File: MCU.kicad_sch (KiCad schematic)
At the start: 87 parts, among them J301 Conn_ARM_JTAG_SWD_20, U1 W9825G6KH-6, U12 USBLC6-2P6, U15 ISOM8115, U18 STM32H7R7I8Tx, U2 W25Q128JVS, U3 FM24CL64B, U301 STM32N657I0H3Q, Y1 ASDLJ-E-49.152MHZ-L-R-T

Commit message: imrt1176 is added
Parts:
- removed C112, C113, C114, C115, C149, C150, C151, C152: 2.2uF, PCM_JLCPCB:C_0402, symbol PCM_JLCPCB-Capacitors:0402,2.2uF
- removed C116, C118, C127, C58, C64, C73: 1uF, PCM_JLCPCB:C_0402, symbol PCM_JLCPCB-Capacitors:0402,1uF
- removed C117, C119, C121, C122, C123, C124, C125, C126, C128, C130, C132, C133, C134, C136, C137, C138, C140, C141, C142, C143, C144, C145, C146, C59, C76, C77: 100nF, PCM_JLCPCB:C_0402, symbol PCM_JLCPCB-Capacitors:0402,100nF
- removed C120, C135, C139, C148: 4.7uF, PCM_JLCPCB:C_0402, symbol PCM_JLCPCB-Capacitors:0402,4.7uF
- removed C147, C153: 10uF, PCM_JLCPCB:C_0603, symbol PCM_JLCPCB-Capacitors:0603,10uF
- removed C154: 220pF, PCM_JLCPCB:C_0402, symbol PCM_JLCPCB-Capacitors:0402,220pF
- removed D2: SMF6.0CA, PCM_JLCPCB:D_SOD-123FL, symbol PCM_JLCPCB-Diodes:TVS-Bi,SMF6.0CA
- removed J301: Conn_ARM_JTAG_SWD_20, Connector_PinSocket_1.27mm:PinSocket_2x10_P1.27mm_Horizontal, symbol Connector:Conn_ARM_JTAG_SWD_20
- removed L1: Choke_Wurth_WE-CNSW_744232090, Inductor_SMD:L_CommonMode_Wurth_WE-CNSW-1206, symbol Filter:Choke_Wurth_WE-CNSW_744232090
- removed L6: 2.2u, Inductor_SMD:L_1206_3216Metric, symbol Device:L
- removed NT1, NT10, NT3, NT4, NT5, NT6, NT7, NT8, NT9: ~, NetTie:NetTie-2_SMD_Pad0.5mm, symbol Device:NetTie_2
- removed R1: 0Ω, PCM_JLCPCB:R_0402, symbol PCM_JLCPCB-Resistors:0402,0Ω
- removed R10, R11: 56kΩ, PCM_JLCPCB:R_0402, symbol PCM_JLCPCB-Resistors:0402,56kΩ
- removed R2: 220Ω, PCM_JLCPCB:R_0805, symbol PCM_JLCPCB-Resistors:0805,220Ω
- removed R35, R40, R45: 33Ω, PCM_JLCPCB:R_0402, symbol PCM_JLCPCB-Resistors:0402,33Ω
- removed R36: 4.7kΩ, PCM_JLCPCB:R_0402, symbol PCM_JLCPCB-Resistors:0402,4.7kΩ
- removed R39: 10kΩ, PCM_JLCPCB:R_0402, symbol PCM_JLCPCB-Resistors:0402,10kΩ
- removed R5: 2kΩ, PCM_JLCPCB:R_0402, symbol PCM_JLCPCB-Resistors:0402,2kΩ
- removed R98: 47Ω, PCM_JLCPCB:R_0402, symbol PCM_JLCPCB-Resistors:0402,47Ω
- removed U15: ISOM8115, Package_SO:SOIC-4_4.55x2.6mm_P1.27mm, symbol Isolator:EL814
- removed U18: STM32H7R7I8Tx, Package_QFP:LQFP-176_24x24mm_P0.5mm, symbol MCU_ST_STM32H7:STM32H7R7I8Tx
- removed U301: STM32N657I0H3Q, User:VFBGA178_12X12_STM, symbol User:STM32N657I0H3Q
- added C15, C16, C59: 1uF, PCM_JLCPCB:C_0402, symbol PCM_JLCPCB-Capacitors:0402,1uF
- added R1, R15: 5.1kΩ, PCM_JLCPCB:R_0402, symbol PCM_JLCPCB-Resistors:0402,5.1kΩ
- added R9: 4.7kΩ, PCM_JLCPCB:R_0402, symbol PCM_JLCPCB-Resistors:0402,4.7kΩ
- added U10: ISOUSB111DWXR, symbol User:ISOUSB111DWXR
- added U6: MIMXRT1176CVM8A, User:BGA289C80P17X17_1400X1400X152, symbol User:MIMXRT1176CVM8A
- added Y3: SG-5032CAN 24MHz, Oscillator:Oscillator_SMD_SeikoEpson_SG8002LB-4Pin_5.0x3.2mm, symbol Oscillator:SG-5032CAN
- Y1: value ASDLJ-E-49.152MHZ-L-R-T -> ASDLJ-E-24.576MHZ-L-R-T
- renumbered C155 to C46, C10 to C57, R116 to R13, R15 to R14, R19 to R16
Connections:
- net +3.3V: now also C15.2, C16.2, U10.14 (3.3V2), U10.16 (VBUS2), Y3.1 (~{ST}), Y3.4 (VCC)
- net CC: now also R15.1
- net D+: now also U12.4 (I/O2); no longer U12.6 (I/O1)
- net D-: now also U12.6 (I/O1); no longer U12.4 (I/O2)
- net FLASH_CLK: now also U6.G14 (GPIO_SD_B2_07)
- net FLASH_QSPI0: now also U6.F15 (GPIO_SD_B2_08)
- net FLASH_QSPI1: now also U6.H15 (GPIO_SD_B2_09)
- net FLASH_QSPI2: now also U6.H14 (GPIO_SD_B2_10)
- net FLASH_QSPI3: now also U6.F16 (GPIO_SD_B2_11)
- net FLASH_~{CS}: now also U6.F17 (GPIO_SD_B2_06)
- net GND: now also C15.1, C16.1, R9.2, U10.15 (GND2), U10.9 (GND2), Y3.2 (GND); no longer C14.2, U12.2 (GND)
- net I2S_CK: now also U6.K12 (GPIO_AD_22)
- net I2S_WS: now also U6.J12 (GPIO_AD_23)
- net RAM_A0: now also U6.A3 (GPIO_EMC_B1_09)
- net RAM_A1: now also U6.A2 (GPIO_EMC_B1_10)
- net RAM_A10: now also U6.B2 (GPIO_EMC_B1_23)
- net RAM_A11: now also U6.C4 (GPIO_EMC_B1_19)
- net RAM_A12: now also U6.C3 (GPIO_EMC_B1_20)
- net RAM_A2: now also U6.C2 (GPIO_EMC_B1_11)
- net RAM_A3: now also U6.C5 (GPIO_EMC_B1_12)
- net RAM_A4: now also U6.D5 (GPIO_EMC_B1_13)
- net RAM_A5: now also U6.B1 (GPIO_EMC_B1_14)
- net RAM_A6: now also U6.C1 (GPIO_EMC_B1_15)
- net RAM_A7: now also U6.D3 (GPIO_EMC_B1_16)
- net RAM_A8: now also U6.B3 (GPIO_EMC_B1_17)
- net RAM_A9: now also U6.B4 (GPIO_EMC_B1_18)
- net RAM_BA0: now also U6.G2 (GPIO_EMC_B1_21)
- net RAM_BA1: now also U6.H2 (GPIO_EMC_B1_22)
- net RAM_CKE: now also U6.G5 (GPIO_EMC_B1_27)
- net RAM_CLK: now also U6.J3 (GPIO_EMC_B1_26)
- net RAM_D0: now also U6.F3 (GPIO_EMC_B1_00)
- net RAM_D1: now also U6.F2 (GPIO_EMC_B1_01)
- net RAM_D10: now also U6.D1 (GPIO_EMC_B1_32)
- net RAM_D11: now also U6.E2 (GPIO_EMC_B1_33)
- net RAM_D12: now also U6.E1 (GPIO_EMC_B1_34)
- net RAM_D13: now also U6.F1 (GPIO_EMC_B1_35)
- net RAM_D14: now also U6.G1 (GPIO_EMC_B1_36)
- net RAM_D15: now also U6.H1 (GPIO_EMC_B1_37)
- net RAM_D2: now also U6.G4 (GPIO_EMC_B1_02)
- net RAM_D3: now also U6.E4 (GPIO_EMC_B1_03)
- net RAM_D4: now also U6.H5 (GPIO_EMC_B1_04)
- net RAM_D5: now also U6.F4 (GPIO_EMC_B1_05)
- net RAM_D6: now also U6.H4 (GPIO_EMC_B1_06)
- net RAM_D7: now also U6.H3 (GPIO_EMC_B1_07)
- net RAM_D8: now also U6.E3 (GPIO_EMC_B1_30)
- net RAM_D9: now also U6.D2 (GPIO_EMC_B1_31)
- net RAM_DQMH: now also U6.J1 (GPIO_EMC_B1_38)
- net RAM_DQML: now also U6.F5 (GPIO_EMC_B1_08)
- net RAM_~{CAS}: now also U6.J5 (GPIO_EMC_B1_24)
- net RAM_~{CS}: now also U6.E6 (GPIO_EMC_B1_29)
- net RAM_~{RAS}: now also U6.J4 (GPIO_EMC_B1_25)
- net RAM_~{WE}: now also U6.E5 (GPIO_EMC_B1_28)
- net VBUS: now also C59.1, U10.1 (VBUS1); no longer C14.1
- net VBUS_DETECT: now also U10.12 (V1OK), U6.D17 (USB1_VBUS)
- net VCONN: now also R1.1
- net AUDIOCLK: now reaches Y1.3 (Out)
- net AUDIOCLK: now also U6.N15 (GPIO_AD_17)
- net at U12.1 (I/O1): now also U10.6 (UD-)
- net at U12.3 (I/O2): now also U10.7 (UD+)
- new net: C14.1, U10.3 (3.3V1)
- new net D_iso+: U10.10 (DD+), U6.E17 (USB1_DP)
- new net D_iso-: U10.11 (DD-), U6.E16 (USB1_DN)
- new net ENC1_PHASE_A: U6.R1 (GPIO_EMC_B2_03)
- new net ENC1_PHASE_B: U6.P1 (GPIO_EMC_B2_08)
- new net I2S_RX: U6.K13 (GPIO_AD_20)
- new net I2S_TX: U6.K14 (GPIO_AD_21)
- new net ISO_GND: C14.2, C59.2, R1.2, R15.2, U10.2 (GND1), U10.8 (GND1), U12.2 (GND)
- new net JTAG_MOD: R9.1, U6.U6 (GPIO_LPSR_13)
- new net JTAG_TCK: U6.T6 (GPIO_LPSR_14)
- new net JTAG_TDI: U6.U5 (GPIO_LPSR_12)
- new net JTAG_TDO: U6.T5 (GPIO_LPSR_11)
- new net JTAG_TMS: U6.U7 (GPIO_LPSR_15)
- new net JTAG_TRSTB: U6.R5 (GPIO_LPSR_10)
- new net MCU_CLOCK: U6.U16 (XTALI), Y3.3 (OUT)
- new net SPDIF_IN_UNUSED: U6.D9 (GPIO_DISP_B2_10)
- new net SPDIF_OUT_UNUSED: U6.A6 (GPIO_DISP_B2_11)
- no-connect marks 2 -> 9
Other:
- moved on the sheet: C46, C57, R117, R13, R14, R16, U12, U2, Y1

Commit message: added renesas RA8P1
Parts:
- removed C46, C67: 100nF, PCM_JLCPCB:C_0402, symbol PCM_JLCPCB-Capacitors:0402,100nF
- removed R117: 10kΩ, PCM_JLCPCB:R_0402, symbol PCM_JLCPCB-Resistors:0402,10kΩ
- removed R9: 4.7kΩ, PCM_JLCPCB:R_0402, symbol PCM_JLCPCB-Resistors:0402,4.7kΩ
- removed U2: W25Q128JVS, Package_SO:SOIC-8_5.3x5.3mm_P1.27mm, symbol Memory_Flash:W25Q128JVS
- removed U6: MIMXRT1176CVM8A, User:BGA289C80P17X17_1400X1400X152, symbol User:MIMXRT1176CVM8A
- added C46, C67, C76, C77, C78, C80: 4.7uF, PCM_JLCPCB:C_0402, symbol PCM_JLCPCB-Capacitors:0402,4.7uF
- added IC2: R7KA8P1KFLCAB#UC0, User:BGA-225_15x15_11.0x11.0mm, symbol User:R7KA8P1KFLCAB#UC0
- added JP1: BOOT_Sel, Jumper:SolderJumper-2_P1.3mm_Open_RoundedPad1.0x1.5mm, symbol Jumper:SolderJumper_2_Open
- added R31: 10kΩ, PCM_JLCPCB:R_0402, symbol PCM_JLCPCB-Resistors:0402,10kΩ
- added R34: 1.5kΩ, PCM_JLCPCB:R_0402, symbol PCM_JLCPCB-Resistors:0402,1.5kΩ
- added R55: 10kΩ, PCM_JLCPCB:R_0402x4, symbol PCM_JLCPCB-Resistors:0402x4,10kΩ
- added U2: IS25LX512M-JHLE, Package_BGA:BGA-24_6x8mm_Layout5x5_P1.0mm, symbol User:IS25LX512M-JHLE
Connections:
- net +3.3V: now also R14.2, C46.1, C67.1, C76.1, C77.1, C78.1, C80.1, R31.1, R55.1, R55.2, R55.3, R55.4, U2.B4 (VCC), U2.D1 (VCC), U2.E4 (VCC); no longer R14.1
- net AUDIOCLK: now also IC2.D9 (AUDIO_CLK)
- net D_iso+: now also IC2.R14 (P814/USB_DP)
- net D_iso-: now also IC2.P14 (P815/USB_DM)
- net FLASH_CLK: now also IC2.R5 (OSPI_CLK), U2.B2 (CLK)
- net FLASH_~{CS}: now also IC2.L4 (OSPI_CS0), R55.5, U2.C2 (~{CS})
- net FRAM_SCL: now also R14.1, IC2.L12 (FRAM_SCL0); no longer R16.2
- net FRAM_SDA: now also R16.2, IC2.L10 (FRAM_SDA0); no longer R14.2
- net FRAM_WP: now also IC2.L11 (P414)
- net Footswitch_1: now also IC2.R10 (ADC1_8)
- net Footswitch_2: now also IC2.M9 (ADC1_7)
- net GND: now also C46.2, C67.2, C76.2, C77.2, C78.2, C80.2, R34.2, U2.B3 (VSS), U2.C1 (VSS), U2.E5 (VSS)
- net GPO: now also IC2.F11 (P700)
- net I2S_CK: now also IC2.H11 (I2S_BCK0)
- net I2S_RX: now also IC2.E14 (I2S_RXD0)
- net I2S_TX: now also IC2.E11 (I2S_TXD0)
- net I2S_WS: now also IC2.G11 (I2S_LRCK0)
- net JTAG_TCK: now also IC2.C8 (P211/TCK/SWCLK)
- net JTAG_TDI: now also IC2.D6 (P208/TDI)
- net JTAG_TDO: now also IC2.D8 (P209/TDO/SWO)
- net JTAG_TMS: now also IC2.C7 (P210/TMS/SWDIO)
- net MCU_CLOCK: now also IC2.J15 (P212/EXTAL)
- net Potentiometer_1: now also IC2.R12 (ADC0_0)
- net Potentiometer_2: now also IC2.N11 (ADC0_1)
- net Potentiometer_3: now also IC2.P11 (ADC0_2)
- net Potentiometer_4: now also IC2.P12 (ADC0_3)
- net Potentiometer_5: now also IC2.R11 (ADC0_4)
- net Potentiometer_6: now also IC2.N10 (ADC0_5)
- net RAM_A0: now also IC2.G1 (SDRAM_A1)
- net RAM_A1: now also IC2.G4 (SDRAM_A2)
- net RAM_A10: now also IC2.J4 (SDRAM_A11)
- net RAM_A11: now also IC2.K4 (SDRAM_A12)
- net RAM_A12: now also IC2.J2 (SDRAM_A13)
- net RAM_A2: now also IC2.G2 (SDRAM_A3)
- net RAM_A3: now also IC2.G3 (SDRAM_A4)
- net RAM_A4: now also IC2.H1 (SDRAM_A5)
- net RAM_A5: now also IC2.H2 (SDRAM_A7)
- net RAM_A6: now also IC2.H3 (SDRAM_A6)
- net RAM_A7: now also IC2.H4 (SDRAM_A8)
- net RAM_A8: now also IC2.J1 (SDRAM_A9)
- net RAM_A9: now also IC2.J3 (SDRAM_A10)
- net RAM_BA0: now also IC2.K2 (SDRAM_A14)
- net RAM_BA1: now also IC2.K3 (SDRAM_A15)
- net RAM_CKE: now also IC2.F1 (SDRAM_CKE)
- net RAM_CLK: now also IC2.E1 (SDRAM_SDCLK)
- net RAM_D0: now also IC2.B5 (SDRAM_DQ0)
- net RAM_D1: now also IC2.C5 (SDRAM_DQ1)
- net RAM_D10: now also IC2.C3 (SDRAM_DQ10)
- net RAM_D11: now also IC2.D4 (SDRAM_DQ11)
- net RAM_D12: now also IC2.B1 (SDRAM_DQ12)
- net RAM_D13: now also IC2.C2 (SDRAM_DQ13)
- net RAM_D14: now also IC2.C1 (SDRAM_DQ14)
- net RAM_D15: now also IC2.D2 (SDRAM_DQ15)
- net RAM_D2: now also IC2.A5 (SDRAM_DQ2)
- net RAM_D3: now also IC2.A4 (SDRAM_DQ3)
- net RAM_D4: now also IC2.B4 (SDRAM_DQ4)
- net RAM_D5: now also IC2.A3 (SDRAM_DQ5)
- net RAM_D6: now also IC2.B3 (SDRAM_DQ6)
- net RAM_D7: now also IC2.C4 (SDRAM_DQ7)
- net RAM_D8: now also IC2.A2 (SDRAM_DQ8)
- net RAM_D9: now also IC2.B2 (SDRAM_DQ9)
- net RAM_DQMH: now also IC2.F3 (SDRAM_DQM1)
- net RAM_DQML: now also IC2.D3 (SDRAM_DQM0)
- net RAM_~{CAS}: now also IC2.E4 (SDRAM_CAS)
- net RAM_~{CS}: now also IC2.E3 (SDRAM_SDCS)
- net RAM_~{RAS}: now also IC2.F2 (SDRAM_RAS)
- net RAM_~{WE}: now also IC2.E2 (SDRAM_WE)
- net Switch_1A: now also IC2.M8 (ADC1_9)
- net Switch_1B: now also IC2.P10 (ADC1_6)
- net Switch_2A: now also IC2.R7 (ADC0_14)
- net Switch_2B: now also IC2.P7 (ADC1_15)
- net VBUS_DETECT: now also IC2.K12 (P407/USB_VBUS)
- net ~{RESET}: now also IC2.C6 (RES)
- new net: JP1.1 (A), R34.1
- new net BOOT_MODE: IC2.D7 (P201/MD), JP1.2 (B), R31.2
- new net FLASH_DS: IC2.M6 (OSPI_DQS), U2.C3 (DS)
- new net FLASH_OSPI0: IC2.R6 (OSPI_D0), U2.D3 (D0)
- new net FLASH_OSPI1: IC2.M7 (OSPI_D1), U2.D2 (D1)
- new net FLASH_OSPI2: IC2.N4 (OSPI_D2), U2.C4 (D2)
- new net FLASH_OSPI3: IC2.N5 (OSPI_D3), U2.D4 (D3)
- new net FLASH_OSPI4: IC2.M5 (OSPI_D4), U2.D5 (D4)
- new net FLASH_OSPI5: IC2.P6 (OSPI_D5), U2.E3 (D5)
- new net FLASH_OSPI6: IC2.N6 (OSPI_D6), U2.E2 (D6)
- new net FLASH_OSPI7: IC2.N7 (OSPI_D7), U2.E1 (D7)
- new net FLASH_~{INT}: IC2.L7 (OSPI_ECSINT1), R55.6, U2.A5 (~{INT})
- new net FLASH_~{RST}: IC2.L5 (OSPI_RESET), R55.7, R55.8, U2.A4 (~{RST})
- no-connect marks 9 -> 20
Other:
- note added: "0: USB boot 1: JTAG/Flash boot"
- note removed: "3.3V - 25mA"
- moved on the sheet: C57, R13, R14, R15, R16, Y1, Y3

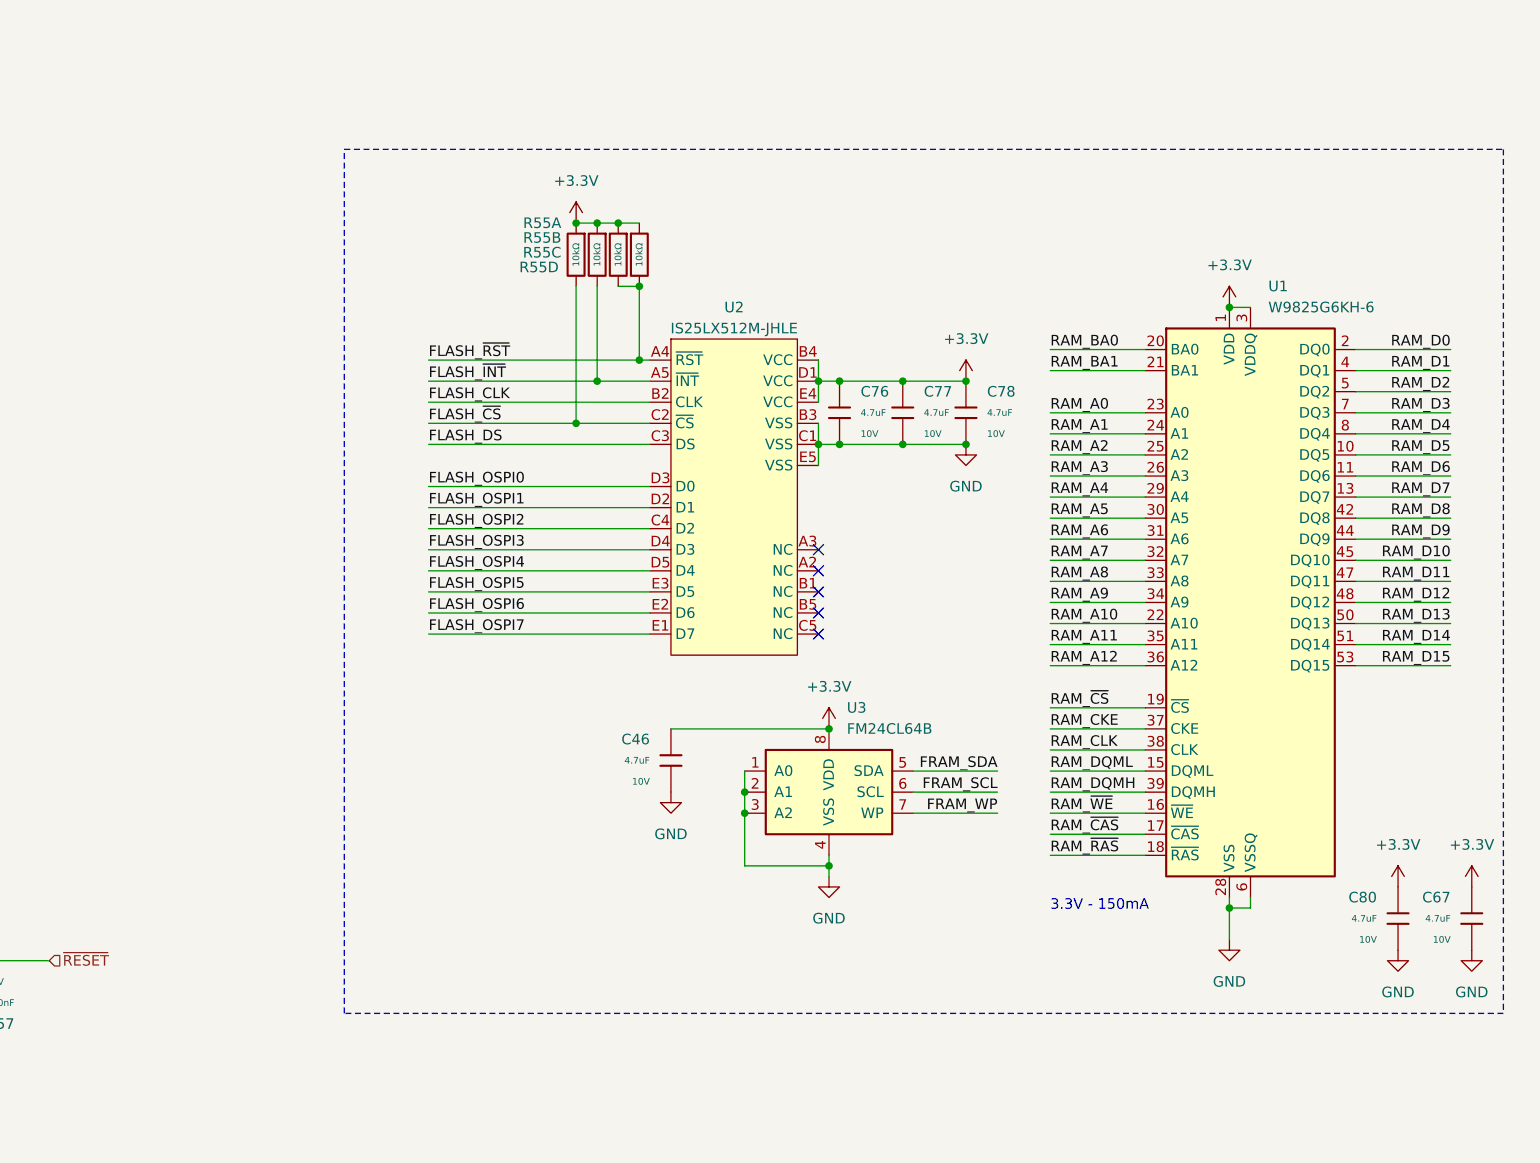
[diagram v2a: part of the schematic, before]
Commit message: progressed with SDRAM layout
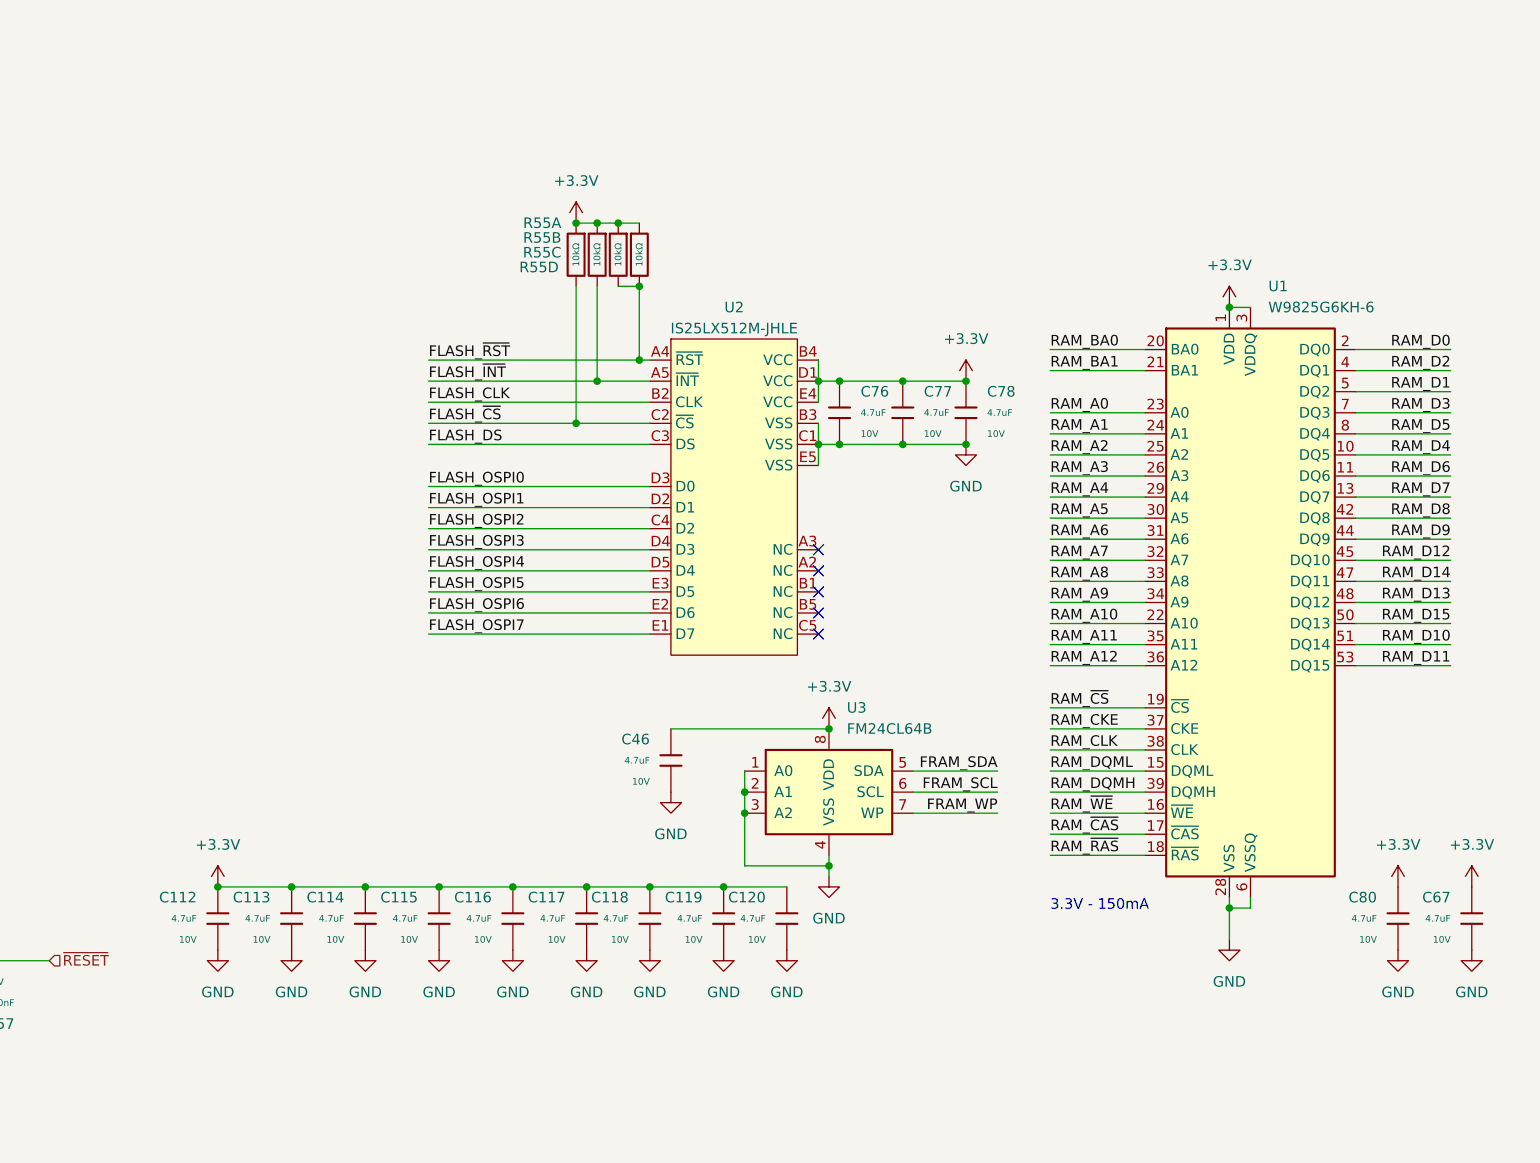
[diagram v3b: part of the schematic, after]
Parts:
- added C112, C113, C114, C115, C116, C117, C118, C119, C120: 4.7uF, PCM_JLCPCB:C_0402, symbol PCM_JLCPCB-Capacitors:0402,4.7uF
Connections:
- net +3.3V: now also C112.1, C113.1, C114.1, C115.1, C116.1, C117.1, C118.1, C119.1, C120.1
- net GND: now also C112.2, C113.2, C114.2, C115.2, C116.2, C117.2, C118.2, C119.2, C120.2
- net RAM_D1: now also U1.5 (DQ2); no longer U1.4 (DQ1)
- net RAM_D10: now also U1.51 (DQ14); no longer U1.45 (DQ10)
- net RAM_D11: now also U1.53 (DQ15); no longer U1.47 (DQ11)
- net RAM_D12: now also U1.45 (DQ10); no longer U1.48 (DQ12)
- net RAM_D13: now also U1.48 (DQ12); no longer U1.50 (DQ13)
- net RAM_D14: now also U1.47 (DQ11); no longer U1.51 (DQ14)
- net RAM_D15: now also U1.50 (DQ13); no longer U1.53 (DQ15)
- net RAM_D2: now also U1.4 (DQ1); no longer U1.5 (DQ2)
- net RAM_D4: now also U1.10 (DQ5); no longer U1.8 (DQ4)
- net RAM_D5: now also U1.8 (DQ4); no longer U1.10 (DQ5)

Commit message: layout progress
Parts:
- removed C46: 4.7uF, PCM_JLCPCB:C_0402, symbol PCM_JLCPCB-Capacitors:0402,4.7uF
- added C88: 1uF, PCM_JLCPCB:C_0402, symbol PCM_JLCPCB-Capacitors:0402,1uF
- added D11, D12, D13, D14, D15, D16, D17, D18, D19: H5VL10B, PCM_JLCPCB:D_DFN1006-2L, symbol PCM_JLCPCB-Diodes:TVS-Bi,H5VL10B
- added J1: UI Board Connector, Connector_SMD_Wurth:J_Wurth_WR-MM_690367280676, symbol Connector_Generic:Conn_01x06
- added R29: 47Ω, PCM_JLCPCB:R_0402, symbol PCM_JLCPCB-Resistors:0402,47Ω
- U10: footprint (none) -> User:SOIC16_DW_TEX-L
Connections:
- net +3.3V: now also D16.1, D19.1, J1.5 (Pin_5)
- net D+: now also U12.6 (I/O1); no longer U12.4 (I/O2)
- net D-: now also U12.4 (I/O2); no longer U12.6 (I/O1)
- net FLASH_~{INT}: now also R55.8; no longer R55.6
- net FLASH_~{RST}: now also R55.6; no longer R55.8
- net GND: now also D11.2, D12.2, D13.2, D14.2, D15.2, D16.2, D17.1, D18.2, D19.2, J1.2 (Pin_2), J1.4 (Pin_4), J1.6 (Pin_6)
- net ISO_GND: now also C88.2
- net JTAG_TCK: now also D14.1
- net JTAG_TDI: now also D13.1
- net JTAG_TDO: now also D12.1
- net JTAG_TMS: now also D15.1
- net VBUS: now also C88.1
- net ~{RESET}: now also D11.1
- net ~{Analog_Dry}: now reaches IC2.A15 (P206)
- net at IC2.D14 (UART_TXD1): now also R29.1
- net UART_RX: now reaches IC2.D15 (UART_RXD1)
- net UART_RX: now also D17.2, J1.3 (Pin_3)
- net UD+: now reaches U12.1 (I/O1)
- net UD+: now also U10.7 (UD+); no longer U10.6 (UD-)
- net UD-: now reaches U12.3 (I/O2)
- net UD-: now also U10.6 (UD-); no longer U10.7 (UD+)
- net Footswitch_1: no longer names the net of IC2.R10 (ADC1_8)
- net Footswitch_2: no longer names the net of IC2.M9 (ADC1_7)
- net Potentiometer_1: no longer names the net of IC2.R12 (ADC0_0)
- net Potentiometer_2: no longer names the net of IC2.N11 (ADC0_1)
- net Potentiometer_3: no longer names the net of IC2.P11 (ADC0_2)
- net Potentiometer_4: no longer names the net of IC2.P12 (ADC0_3)
- net Potentiometer_5: no longer names the net of IC2.R11 (ADC0_4)
- net Potentiometer_6: no longer names the net of IC2.N10 (ADC0_5)
- net Switch_1A: no longer names the net of IC2.M8 (ADC1_9)
- net Switch_1B: no longer names the net of IC2.P10 (ADC1_6)
- net Switch_2A: no longer names the net of IC2.R7 (ADC0_14)
- net Switch_2B: no longer names the net of IC2.P7 (ADC1_15)
- new net UART_TX: D18.1, J1.1 (Pin_1), R29.2
- no-connect marks 20 -> 21
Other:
- note added: "ADD load switch!!!"
- note added: "Additional Decoupling"
- note added: "Audio + SYS clocks"
- note added: "External Board connector"
- note added: "Isolated USB"
- note added: "MCU FLASH+SDRAM+I2S"
- note added: "MCU GPIO"
- note added: "OctoSPI Flash"
- note added: "Parallel SDRAM"
- note added: "Preset FRAM"
- note added: "TPS22919"
- note added: "USB+SWD"
- company: (none) -> KVAD
- title: (none) -> Project Y
- moved on the sheet: C112, C113, C114, C115, C116, C117, C118, C119, C120, C14, C15, C16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
